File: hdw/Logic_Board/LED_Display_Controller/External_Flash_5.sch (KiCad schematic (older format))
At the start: 16 parts, among them U2201 SST25PF020B

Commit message: Added some digikey partnumbers to components
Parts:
- C2201: footprint (none) -> Capacitors_SMD:C_0603; Digi-Key PN PN -> 311-1344-1-ND; Voltage 25V -> 50V
- C2202: Digi-Key PN PN -> 1276-1921-1-ND; Voltage 25V -> 50V
- C2203: Digi-Key PN PN -> 1276-1018-1-ND; Voltage 25V -> 50V
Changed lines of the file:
@@
 F 0 "C2201" H 5815 5530 50  0000 L CNN
 F 1 "0.1uF" H 5815 5330 50  0000 L CNN
-F 2 "" H 5828 5280 50  0001 C CNN
+F 2 "Capacitors_SMD:C_0603" H 5828 5280 50  0001 C CNN
 F 3 "" H 5815 5530 50  0001 C CNN
 F 4 "0603" H 5640 5530 50  0000 R CNN "display_footprint"
-F 5 "25V" H 5640 5430 50  0000 R CNN "Voltage"
+F 5 "50V" H 5640 5430 50  0000 R CNN "Voltage"
 F 6 "X7R" H 5640 5330 50  0000 R CNN "Dielectric"
-F 7 "PN" H 6215 5930 60  0001 C CNN "Digi-Key PN"
+F 7 "311-1344-1-ND" H 6215 5930 60  0001 C CNN "Digi-Key PN"
 	1    5790 5430
 	1    0    0    -1
@@
 F 3 "" H 6115 5530 50  0001 C CNN
 F 4 "0603" H 5940 5530 50  0001 R CNN "display_footprint"
-F 5 "25V" H 5940 5430 50  0001 R CNN "Voltage"
+F 5 "50V" H 5940 5430 50  0001 R CNN "Voltage"
 F 6 "X7R" H 5940 5330 50  0001 R CNN "Dielectric"
-F 7 "PN" H 6515 5930 60  0001 C CNN "Digi-Key PN"
+F 7 "1276-1921-1-ND" H 6515 5930 60  0001 C CNN "Digi-Key PN"
 	1    6090 5430
 	1    0    0    -1
@@
 F 3 "" H 6415 5530 50  0001 C CNN
 F 4 "0603" H 6240 5530 50  0001 R CNN "display_footprint"
-F 5 "25V" H 6240 5430 50  0001 R CNN "Voltage"
+F 5 "50V" H 6240 5430 50  0001 R CNN "Voltage"
 F 6 "X7R" H 6240 5330 50  0001 R CNN "Dielectric"
-F 7 "PN" H 6815 5930 60  0001 C CNN "Digi-Key PN"
+F 7 "1276-1018-1-ND" H 6815 5930 60  0001 C CNN "Digi-Key PN"
 	1    6390 5430
 	1    0    0    -1

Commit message: Finished first pass of digikey part numbers
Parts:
- R2201, R2202, R2203, R2204, R2205, R2212: Digi-Key PN PN -> A106047CT-ND
- R2206, R2207, R2208, R2209, R2210, R2211: Digi-Key PN PN -> RMCF0603FT10K0CT-ND
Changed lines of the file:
@@
 F 5 "1%" H 5410 4320 50  0000 L CNN "Tolerance"
 F 6 "1/10W" H 5410 4240 50  0000 L CNN "Wattage"
-F 7 "PN" H 5630 4720 60  0001 C CNN "Digi-Key PN"
+F 7 "RMCF0603FT10K0CT-ND" H 5630 4720 60  0001 C CNN "Digi-Key PN"
 	1    5330 4320
 	1    0    0    -1
@@
 F 5 "1%" H 4600 4320 50  0000 L CNN "Tolerance"
 F 6 "1/10W" H 4600 4240 50  0000 L CNN "Wattage"
-F 7 "PN" H 4820 4720 60  0001 C CNN "Digi-Key PN"
+F 7 "RMCF0603FT10K0CT-ND" H 4820 4720 60  0001 C CNN "Digi-Key PN"
 	1    4520 4320
 	1    0    0    -1
@@
 F 5 "1%" H 5190 3130 50  0000 L CNN "Tolerance"
 F 6 "1/10W" H 5190 3050 50  0000 L CNN "Wattage"
-F 7 "PN" H 5410 3530 60  0001 C CNN "Digi-Key PN"
+F 7 "RMCF0603FT10K0CT-ND" H 5410 3530 60  0001 C CNN "Digi-Key PN"
 	1    5110 3130
 	1    0    0    -1
@@
 F 5 "1%" H 4600 3130 50  0000 L CNN "Tolerance"
 F 6 "1/10W" H 4600 3050 50  0000 L CNN "Wattage"
-F 7 "PN" H 4820 3530 60  0001 C CNN "Digi-Key PN"
+F 7 "RMCF0603FT10K0CT-ND" H 4820 3530 60  0001 C CNN "Digi-Key PN"
 	1    4520 3130
 	1    0    0    -1
@@
 F 5 "1%" H 4010 3130 50  0000 L CNN "Tolerance"
 F 6 "1/10W" H 4010 3050 50  0000 L CNN "Wattage"
-F 7 "PN" H 4230 3530 60  0001 C CNN "Digi-Key PN"
+F 7 "RMCF0603FT10K0CT-ND" H 4230 3530 60  0001 C CNN "Digi-Key PN"
 	1    3930 3130
 	1    0    0    -1
@@
 F 5 "1%" H 6830 3850 50  0000 L CNN "Tolerance"
 F 6 "1/10W" H 6830 3770 50  0000 L CNN "Wattage"
-F 7 "PN" H 7050 4250 60  0001 C CNN "Digi-Key PN"
+F 7 "RMCF0603FT10K0CT-ND" H 7050 4250 60  0001 C CNN "Digi-Key PN"
 	1    6750 3850
 	1    0    0    -1
@@
 F 5 "1%" V 3620 3450 50  0001 C CNN "Tolerance"
 F 6 "1/10W" V 3720 3450 50  0001 C CNN "Wattage"
-F 7 "PN" H 3720 3850 60  0001 C CNN "Digi-Key PN"
+F 7 "A106047CT-ND" H 3720 3850 60  0001 C CNN "Digi-Key PN"
 	1    3420 3450
 	0    1    1    0
@@
 F 5 "1%" V 7330 3450 50  0001 C CNN "Tolerance"
 F 6 "1/10W" V 7430 3450 50  0001 C CNN "Wattage"
-F 7 "PN" H 7430 3850 60  0001 C CNN "Digi-Key PN"
+F 7 "A106047CT-ND" H 7430 3850 60  0001 C CNN "Digi-Key PN"
 	1    7130 3450
 	0    1    1    0
@@
 F 5 "1%" V 3620 3550 50  0001 C CNN "Tolerance"
 F 6 "1/10W" V 3720 3550 50  0001 C CNN "Wattage"
-F 7 "PN" H 3720 3950 60  0001 C CNN "Digi-Key PN"
+F 7 "A106047CT-ND" H 3720 3950 60  0001 C CNN "Digi-Key PN"
 	1    3420 3550
 	0    1    1    0
@@
 F 5 "1%" V 3620 3750 50  0001 C CNN "Tolerance"
 F 6 "1/10W" V 3720 3750 50  0001 C CNN "Wattage"
-F 7 "PN" H 3720 4150 60  0001 C CNN "Digi-Key PN"
+F 7 "A106047CT-ND" H 3720 4150 60  0001 C CNN "Digi-Key PN"
 	1    3420 3750
 	0    1    1    0
@@
 F 5 "1%" V 3620 3850 50  0001 C CNN "Tolerance"
 F 6 "1/10W" V 3720 3850 50  0001 C CNN "Wattage"
-F 7 "PN" H 3720 4250 60  0001 C CNN "Digi-Key PN"
+F 7 "A106047CT-ND" H 3720 4250 60  0001 C CNN "Digi-Key PN"
 	1    3420 3850
 	0    1    1    0
@@
 F 5 "1%" V 3620 3650 50  0001 C CNN "Tolerance"
 F 6 "1/10W" V 3720 3650 50  0001 C CNN "Wattage"
-F 7 "PN" H 3720 4050 60  0001 C CNN "Digi-Key PN"
+F 7 "A106047CT-ND" H 3720 4050 60  0001 C CNN "Digi-Key PN"
 	1    3420 3650
 	0    1    1    0

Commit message: First pass assignment of footprints to all components
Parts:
- C2202, C2203: footprint (none) -> Capacitors_SMD:C_0603
- R2201, R2202, R2203, R2204, R2205, R2206, R2207, R2208, R2209, R2210, R2211, R2212: footprint (none) -> Resistors_SMD:R_0603
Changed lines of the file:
@@
 F 0 "R2210" H 5270 4320 50  0000 R CNN
 F 1 "10k" V 5330 4320 50  0000 C CNN
-F 2 "" H 5330 4320 50  0001 C CNN
+F 2 "Resistors_SMD:R_0603" H 5330 4320 50  0001 C CNN
 F 3 "" H 5330 4320 50  0001 C CNN
 F 4 "0603" H 5410 4400 50  0000 L CNN "display_footprint"
@@
 F 0 "R2208" H 4460 4320 50  0000 R CNN
 F 1 "10k" V 4520 4320 50  0000 C CNN
-F 2 "" H 4520 4320 50  0001 C CNN
+F 2 "Resistors_SMD:R_0603" H 4520 4320 50  0001 C CNN
 F 3 "" H 4520 4320 50  0001 C CNN
 F 4 "0603" H 4600 4400 50  0000 L CNN "display_footprint"
@@
 F 0 "R2209" H 5050 3130 50  0000 R CNN
 F 1 "10k" V 5110 3130 50  0000 C CNN
-F 2 "" H 5110 3130 50  0001 C CNN
+F 2 "Resistors_SMD:R_0603" H 5110 3130 50  0001 C CNN
 F 3 "" H 5110 3130 50  0001 C CNN
 F 4 "0603" H 5190 3210 50  0000 L CNN "display_footprint"
@@
 F 0 "R2207" H 4460 3130 50  0000 R CNN
 F 1 "10k" V 4520 3130 50  0000 C CNN
-F 2 "" H 4520 3130 50  0001 C CNN
+F 2 "Resistors_SMD:R_0603" H 4520 3130 50  0001 C CNN
 F 3 "" H 4520 3130 50  0001 C CNN
 F 4 "0603" H 4600 3210 50  0000 L CNN "display_footprint"
@@
 F 0 "R2206" H 3870 3130 50  0000 R CNN
 F 1 "10k" V 3930 3130 50  0000 C CNN
-F 2 "" H 3930 3130 50  0001 C CNN
+F 2 "Resistors_SMD:R_0603" H 3930 3130 50  0001 C CNN
 F 3 "" H 3930 3130 50  0001 C CNN
 F 4 "0603" H 4010 3210 50  0000 L CNN "display_footprint"
@@
 F 0 "R2211" H 6690 3850 50  0000 R CNN
 F 1 "10k" V 6750 3850 50  0000 C CNN
-F 2 "" H 6750 3850 50  0001 C CNN
+F 2 "Resistors_SMD:R_0603" H 6750 3850 50  0001 C CNN
 F 3 "" H 6750 3850 50  0001 C CNN
 F 4 "0603" H 6830 3930 50  0000 L CNN "display_footprint"
@@
 F 0 "R2201" V 3380 3580 50  0000 L CNN
 F 1 "100" V 3420 3450 50  0000 C CNN
-F 2 "" H 3420 3450 50  0001 C CNN
+F 2 "Resistors_SMD:R_0603" H 3420 3450 50  0001 C CNN
 F 3 "" H 3420 3450 50  0001 C CNN
 F 4 "0603" V 3520 3450 50  0001 C CNN "display_footprint"
@@
 F 0 "R2212" V 7030 3450 50  0000 C CNN
 F 1 "100" V 7130 3450 50  0000 C CNN
-F 2 "" H 7130 3450 50  0001 C CNN
+F 2 "Resistors_SMD:R_0603" H 7130 3450 50  0001 C CNN
 F 3 "" H 7130 3450 50  0001 C CNN
 F 4 "0603" V 7230 3450 50  0001 C CNN "display_footprint"
@@
 F 0 "C2202" H 6115 5530 50  0000 L CNN
 F 1 "10nF" H 6115 5330 50  0000 L CNN
-F 2 "" H 6128 5280 50  0001 C CNN
+F 2 "Capacitors_SMD:C_0603" H 6128 5280 50  0001 C CNN
 F 3 "" H 6115 5530 50  0001 C CNN
 F 4 "0603" H 5940 5530 50  0001 R CNN "display_footprint"
@@
 F 0 "C2203" H 6415 5530 50  0000 L CNN
 F 1 "1nF" H 6415 5330 50  0000 L CNN
-F 2 "" H 6428 5280 50  0001 C CNN
+F 2 "Capacitors_SMD:C_0603" H 6428 5280 50  0001 C CNN
 F 3 "" H 6415 5530 50  0001 C CNN
 F 4 "0603" H 6240 5530 50  0001 R CNN "display_footprint"
@@
 F 0 "R2202" V 3380 3680 50  0000 L CNN
 F 1 "100" V 3420 3550 50  0000 C CNN
-F 2 "" H 3420 3550 50  0001 C CNN
+F 2 "Resistors_SMD:R_0603" H 3420 3550 50  0001 C CNN
 F 3 "" H 3420 3550 50  0001 C CNN
 F 4 "0603" V 3520 3550 50  0001 C CNN "display_footprint"
@@
 F 0 "R2204" V 3380 3880 50  0000 L CNN
 F 1 "100" V 3420 3750 50  0000 C CNN
-F 2 "" H 3420 3750 50  0001 C CNN
+F 2 "Resistors_SMD:R_0603" H 3420 3750 50  0001 C CNN
 F 3 "" H 3420 3750 50  0001 C CNN
 F 4 "0603" V 3520 3750 50  0001 C CNN "display_footprint"
@@
 F 0 "R2205" V 3380 3980 50  0000 L CNN
 F 1 "100" V 3420 3850 50  0000 C CNN
-F 2 "" H 3420 3850 50  0001 C CNN
+F 2 "Resistors_SMD:R_0603" H 3420 3850 50  0001 C CNN
 F 3 "" H 3420 3850 50  0001 C CNN
 F 4 "0603" V 3520 3850 50  0001 C CNN "display_footprint"
@@
 F 0 "R2203" V 3380 3780 50  0000 L CNN
 F 1 "100" V 3420 3650 50  0000 C CNN
-F 2 "" H 3420 3650 50  0001 C CNN
+F 2 "Resistors_SMD:R_0603" H 3420 3650 50  0001 C CNN
 F 3 "" H 3420 3650 50  0001 C CNN
 F 4 "0603" V 3520 3650 50  0001 C CNN "display_footprint"

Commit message: Resolved a few library dependencies
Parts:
- R2201, R2202, R2203, R2204, R2205, R2206, R2207, R2208, R2209, R2210, R2211, R2212: symbol Custom_Library:R_Custom -> LED_Display_Local_Library:R_Custom
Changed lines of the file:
@@
 $EndComp
 $Comp
-L Custom_Library:R_Custom R2210
+L LED_Display_Local_Library:R_Custom R2210
 U 1 1 5BBE9655
 P 5330 4320
@@
 $EndComp
 $Comp
-L Custom_Library:R_Custom R2208
+L LED_Display_Local_Library:R_Custom R2208
 U 1 1 5BBE9660
 P 4520 4320
@@
 $EndComp
 $Comp
-L Custom_Library:R_Custom R2209
+L LED_Display_Local_Library:R_Custom R2209
 U 1 1 5BBE966B
 P 5110 3130
@@
 $EndComp
 $Comp
-L Custom_Library:R_Custom R2207
+L LED_Display_Local_Library:R_Custom R2207
 U 1 1 5BBE9676
 P 4520 3130
@@
 $EndComp
 $Comp
-L Custom_Library:R_Custom R2206
+L LED_Display_Local_Library:R_Custom R2206
 U 1 1 5BBE9681
 P 3930 3130
@@
 $EndComp
 $Comp
-L Custom_Library:R_Custom R2211
+L LED_Display_Local_Library:R_Custom R2211
 U 1 1 5BBE968C
 P 6750 3850
@@
 $EndComp
 $Comp
-L Custom_Library:R_Custom R2201
+L LED_Display_Local_Library:R_Custom R2201
 U 1 1 5BBE96BB
 P 3420 3450
@@
 FLASH_SCK
 $Comp
-L Custom_Library:R_Custom R2212
+L LED_Display_Local_Library:R_Custom R2212
 U 1 1 5BBE96E8
 P 7130 3450
@@
 	6090 5240 6390 5240
 $Comp
-L Custom_Library:R_Custom R2202
+L LED_Display_Local_Library:R_Custom R2202
 U 1 1 5BBE9733
 P 3420 3550
@@
 $EndComp
 $Comp
-L Custom_Library:R_Custom R2204
+L LED_Display_Local_Library:R_Custom R2204
 U 1 1 5BBE973E
 P 3420 3750
@@
 $EndComp
 $Comp
-L Custom_Library:R_Custom R2205
+L LED_Display_Local_Library:R_Custom R2205
 U 1 1 5BBE9749
 P 3420 3850
@@
 ~FLASH_Hold
 $Comp
-L Custom_Library:R_Custom R2203
+L LED_Display_Local_Library:R_Custom R2203
 U 1 1 5BC1DF14
 P 3420 3650

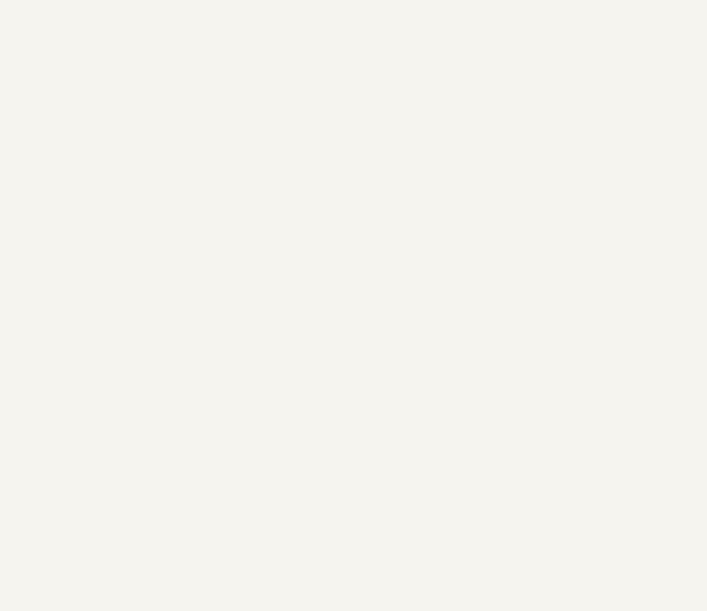
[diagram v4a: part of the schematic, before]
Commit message: Added flash chip select LEDs
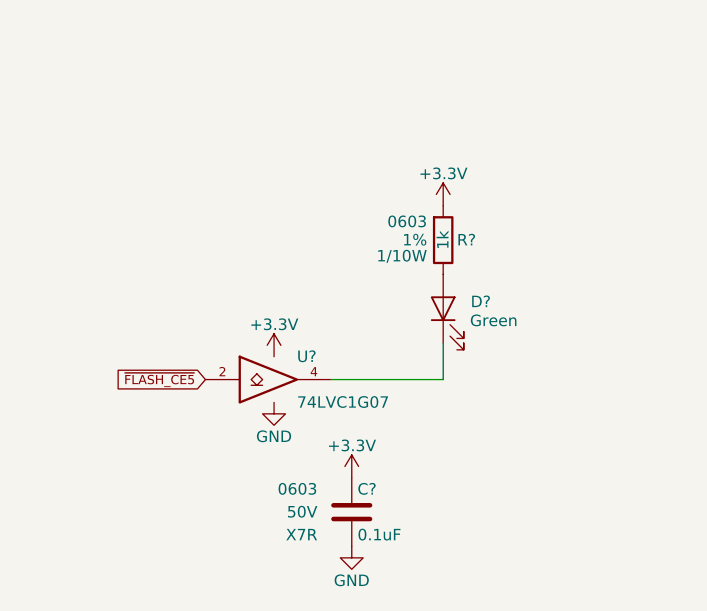
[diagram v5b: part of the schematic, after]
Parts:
- added C?: 0.1uF, Capacitors_SMD:C_0603, symbol LED_Display_Local_Library:C_Custom
- added D?: Green, LEDs:LED_0603, symbol Device:LED
- added R?: 1k, Resistors_SMD:R_0603, symbol LED_Display_Local_Library:R_Custom
- added U?: 74LVC1G07, TO_SOT_Packages_SMD:SOT-353_SC-70-5, symbol LED_Display_Local_Library:74LVC1G07_Power
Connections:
- net +3V3: now also C?.1, R?.1, U?.5 (VCC)
- net GND: now also C?.2, U?.3 (GND)
- net ~FLASH_CE5: now also U?.2
- new net: D?.1 (K), U?.4
- new net: D?.2 (A), R?.2
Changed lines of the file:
@@
 Wire Wire Line
 	4520 3850 5680 3850
+$Comp
+L LED_Display_Local_Library:C_Custom C?
+U 1 1 5C172D4E
+P 2010 6900
+AR Path="/5BAAE16C/5C172D4E" Ref="C?"  Part="1"
+AR Path="/5BB181D8/5C172D4E" Ref="C?"  Part="1"
+AR Path="/5BB2595E/5C172D4E" Ref="C?"  Part="1"
+AR Path="/5BB25AF0/5C172D4E" Ref="C?"  Part="1"
+F 0 "C?" H 2035 7000 50  0000 L CNN
+F 1 "0.1uF" H 2035 6800 50  0000 L CNN
+F 2 "Capacitors_SMD:C_0603" H 2048 6750 50  0001 C CNN
+F 3 "" H 2035 7000 50  0001 C CNN
+F 4 "0603" H 1860 7000 50  0000 R CNN "display_footprint"
+F 5 "50V" H 1860 6900 50  0000 R CNN "Voltage"
+F 6 "X7R" H 1860 6800 50  0000 R CNN "Dielectric"
+F 7 "311-1344-1-ND" H 2435 7400 60  0001 C CNN "Digi-Key PN"
+	1    2010 6900
+	1    0    0    -1
+$EndComp
+$Comp
+L LED_Display_Local_Library:74LVC1G07_Power U?
+U 1 1 5C172D56
+P 1670 6320
+AR Path="/5BB2595E/5C172D56" Ref="U?"  Part="1"
+AR Path="/5BB25AF0/5C172D56" Ref="U?"  Part="1"
+F 0 "U?" H 1770 6420 50  0000 L CNN
+F 1 "74LVC1G07" H 1770 6220 50  0000 L CNN
+F 2 "TO_SOT_Packages_SMD:SOT-353_SC-70-5" H 1670 6320 50  0001 C CNN
+F 3 "http://www.ti.com/lit/sg/scyt129e/scyt129e.pdf" H 1670 6320 50  0001 C CNN
+F 4 "296-8486-1-ND" H 1670 6320 50  0001 C CNN "Digi-Key PN"
+	1    1670 6320
+	1    0    0    -1
+$EndComp
+$Comp
+L power:+3.3V #PWR?
+U 1 1 5C172D5D
+P 1670 6220
+AR Path="/5BB2595E/5C172D5D" Ref="#PWR?"  Part="1"
+AR Path="/5BB25AF0/5C172D5D" Ref="#PWR?"  Part="1"
+F 0 "#PWR?" H 1670 6070 50  0001 C CNN
+F 1 "+3.3V" H 1670 6360 50  0000 C CNN
+F 2 "" H 1670 6220 50  0001 C CNN
+F 3 "" H 1670 6220 50  0001 C CNN
+	1    1670 6220
+	1    0    0    -1
+$EndComp
+$Comp
+L power:+3.3V #PWR?
+U 1 1 5C172D63
+P 2010 6750
+AR Path="/5BB2595E/5C172D63" Ref="#PWR?"  Part="1"
+AR Path="/5BB25AF0/5C172D63" Ref="#PWR?"  Part="1"
+F 0 "#PWR?" H 2010 6600 50  0001 C CNN
+F 1 "+3.3V" H 2010 6890 50  0000 C CNN
+F 2 "" H 2010 6750 50  0001 C CNN
+F 3 "" H 2010 6750 50  0001 C CNN
+	1    2010 6750
+	1    0    0    -1
+$EndComp
+$Comp
+L power:GND #PWR?
+U 1 1 5C172D69
+P 2010 7050
+AR Path="/5BB2595E/5C172D69" Ref="#PWR?"  Part="1"
+AR Path="/5BB25AF0/5C172D69" Ref="#PWR?"  Part="1"
+F 0 "#PWR?" H 2010 6800 50  0001 C CNN
+F 1 "GND" H 2010 6900 50  0000 C CNN
+F 2 "" H 2010 7050 50  0001 C CNN
+F 3 "" H 2010 7050 50  0001 C CNN
+	1    2010 7050
+	1    0    0    -1
+$EndComp
+$Comp
+L power:GND #PWR?
+U 1 1 5C172D6F
+P 1670 6420
+AR Path="/5BB2595E/5C172D6F" Ref="#PWR?"  Part="1"
+AR Path="/5BB25AF0/5C172D6F" Ref="#PWR?"  Part="1"
+F 0 "#PWR?" H 1670 6170 50  0001 C CNN
+F 1 "GND" H 1670 6270 50  0000 C CNN
+F 2 "" H 1670 6420 50  0001 C CNN
+F 3 "" H 1670 6420 50  0001 C CNN
+	1    1670 6420
+	1    0    0    -1
+$EndComp
+Text GLabel 1370 6320 0    40   Input ~ 0
+~FLASH_CE5
+$Comp
+L power:+3.3V #PWR?
+U 1 1 5C172D76
+P 2410 5560
+AR Path="/5BB844FD/5C172D76" Ref="#PWR?"  Part="1"
+AR Path="/5BF346B3/5C172D76" Ref="#PWR?"  Part="1"
+AR Path="/5BB2595E/5C172D76" Ref="#PWR?"  Part="1"
+AR Path="/5BB25AF0/5C172D76" Ref="#PWR?"  Part="1"
+F 0 "#PWR?" H 2410 5410 50  0001 C CNN
+F 1 "+3.3V" H 2410 5700 50  0000 C CNN
+F 2 "" H 2410 5560 50  0001 C CNN
+F 3 "" H 2410 5560 50  0001 C CNN
+	1    2410 5560
+	1    0    0    -1
+$EndComp
+Wire Wire Line
+	1920 6320 2410 6320
+Wire Wire Line
+	2410 6320 2410 6160
+$Comp
+L LED_Display_Local_Library:R_Custom R?
+U 1 1 5C172D82
+P 2410 5710
+AR Path="/5BAAE1F3/5C172D82" Ref="R?"  Part="1"
+AR Path="/5BAAE1DC/5C172D82" Ref="R?"  Part="1"
+AR Path="/5BAAE16C/5C172D82" Ref="R?"  Part="1"
+AR Path="/5BB844FD/5C172D82" Ref="R?"  Part="1"
+AR Path="/5BF346B3/5C172D82" Ref="R?"  Part="1"
+AR Path="/5BB2595E/5C172D82" Ref="R?"  Part="1"
+AR Path="/5BB25AF0/5C172D82" Ref="R?"  Part="1"
+F 0 "R?" H 2350 5710 50  0000 R CNN
+F 1 "1k" V 2410 5710 50  0000 C CNN
+F 2 "Resistors_SMD:R_0603" H 2410 5710 50  0001 C CNN
+F 3 "" H 2410 5710 50  0001 C CNN
+F 4 "0603" H 2480 5790 50  0000 L CNN "display_footprint"
+F 5 "1%" H 2480 5710 50  0000 L CNN "Tolerance"
+F 6 "1/10W" H 2480 5640 50  0000 L CNN "Wattage"
+F 7 "RMCF0603FT1K00CT-ND" H 2710 6110 60  0001 C CNN "Digi-Key PN"
+	1    2410 5710
+	-1   0    0    -1
+$EndComp
+$Comp
+L Device:LED D?
+U 1 1 5C172D8A
+P 2410 6010
+AR Path="/5BB844FD/5C172D8A" Ref="D?"  Part="1"
+AR Path="/5BF346B3/5C172D8A" Ref="D?"  Part="1"
+AR Path="/5BB2595E/5C172D8A" Ref="D?"  Part="1"
+AR Path="/5BB25AF0/5C172D8A" Ref="D?"  Part="1"
+F 0 "D?" V 2440 5890 50  0000 R CNN
+F 1 "Green" V 2357 5893 50  0000 R CNN
+F 2 "LEDs:LED_0603" H 2410 6010 50  0001 C CNN
+F 3 "~" H 2410 6010 50  0001 C CNN
+F 4 "160-1446-1-ND" H -2600 3010 50  0001 C CNN "Digi-Key PN"
+	1    2410 6010
+	0    -1   -1   0
+$EndComp
 $EndSCHEMATC

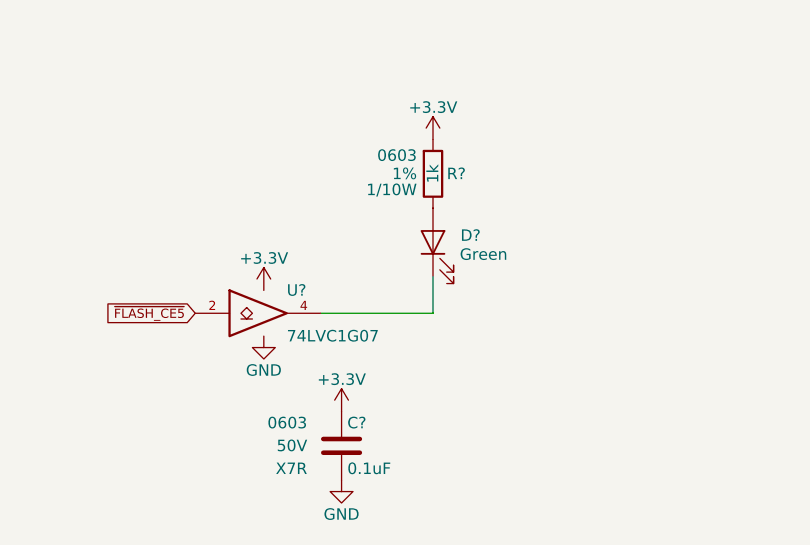
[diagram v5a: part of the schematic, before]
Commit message: Added WIFI comm LED
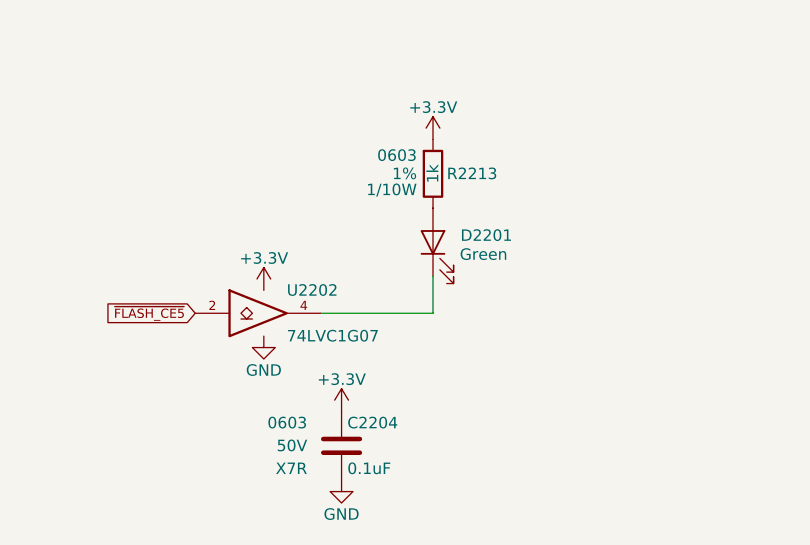
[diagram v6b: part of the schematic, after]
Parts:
- gave numbers to parts that had none: 4
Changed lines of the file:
@@
 AR Path="/5BB181D8/5C172D4E" Ref="C?"  Part="1"
 AR Path="/5BB2595E/5C172D4E" Ref="C?"  Part="1"
-AR Path="/5BB25AF0/5C172D4E" Ref="C?"  Part="1"
-F 0 "C?" H 2035 7000 50  0000 L CNN
+AR Path="/5BB25AF0/5C172D4E" Ref="C2204"  Part="1"
+F 0 "C2204" H 2035 7000 50  0000 L CNN
 F 1 "0.1uF" H 2035 6800 50  0000 L CNN
 F 2 "Capacitors_SMD:C_0603" H 2048 6750 50  0001 C CNN
@@
 P 1670 6320
 AR Path="/5BB2595E/5C172D56" Ref="U?"  Part="1"
-AR Path="/5BB25AF0/5C172D56" Ref="U?"  Part="1"
-F 0 "U?" H 1770 6420 50  0000 L CNN
+AR Path="/5BB25AF0/5C172D56" Ref="U2202"  Part="1"
+F 0 "U2202" H 1770 6420 50  0000 L CNN
 F 1 "74LVC1G07" H 1770 6220 50  0000 L CNN
 F 2 "TO_SOT_Packages_SMD:SOT-353_SC-70-5" H 1670 6320 50  0001 C CNN
@@
 P 1670 6220
 AR Path="/5BB2595E/5C172D5D" Ref="#PWR?"  Part="1"
-AR Path="/5BB25AF0/5C172D5D" Ref="#PWR?"  Part="1"
-F 0 "#PWR?" H 1670 6070 50  0001 C CNN
+AR Path="/5BB25AF0/5C172D5D" Ref="#PWR02211"  Part="1"
+F 0 "#PWR02211" H 1670 6070 50  0001 C CNN
 F 1 "+3.3V" H 1670 6360 50  0000 C CNN
 F 2 "" H 1670 6220 50  0001 C CNN
@@
 P 2010 6750
 AR Path="/5BB2595E/5C172D63" Ref="#PWR?"  Part="1"
-AR Path="/5BB25AF0/5C172D63" Ref="#PWR?"  Part="1"
-F 0 "#PWR?" H 2010 6600 50  0001 C CNN
+AR Path="/5BB25AF0/5C172D63" Ref="#PWR02213"  Part="1"
+F 0 "#PWR02213" H 2010 6600 50  0001 C CNN
 F 1 "+3.3V" H 2010 6890 50  0000 C CNN
 F 2 "" H 2010 6750 50  0001 C CNN
@@
 P 2010 7050
 AR Path="/5BB2595E/5C172D69" Ref="#PWR?"  Part="1"
-AR Path="/5BB25AF0/5C172D69" Ref="#PWR?"  Part="1"
-F 0 "#PWR?" H 2010 6800 50  0001 C CNN
+AR Path="/5BB25AF0/5C172D69" Ref="#PWR02214"  Part="1"
+F 0 "#PWR02214" H 2010 6800 50  0001 C CNN
 F 1 "GND" H 2010 6900 50  0000 C CNN
 F 2 "" H 2010 7050 50  0001 C CNN
@@
 P 1670 6420
 AR Path="/5BB2595E/5C172D6F" Ref="#PWR?"  Part="1"
-AR Path="/5BB25AF0/5C172D6F" Ref="#PWR?"  Part="1"
-F 0 "#PWR?" H 1670 6170 50  0001 C CNN
+AR Path="/5BB25AF0/5C172D6F" Ref="#PWR02212"  Part="1"
+F 0 "#PWR02212" H 1670 6170 50  0001 C CNN
 F 1 "GND" H 1670 6270 50  0000 C CNN
 F 2 "" H 1670 6420 50  0001 C CNN
@@
 AR Path="/5BF346B3/5C172D76" Ref="#PWR?"  Part="1"
 AR Path="/5BB2595E/5C172D76" Ref="#PWR?"  Part="1"
-AR Path="/5BB25AF0/5C172D76" Ref="#PWR?"  Part="1"
-F 0 "#PWR?" H 2410 5410 50  0001 C CNN
+AR Path="/5BB25AF0/5C172D76" Ref="#PWR02215"  Part="1"
+F 0 "#PWR02215" H 2410 5410 50  0001 C CNN
 F 1 "+3.3V" H 2410 5700 50  0000 C CNN
 F 2 "" H 2410 5560 50  0001 C CNN
@@
 AR Path="/5BF346B3/5C172D82" Ref="R?"  Part="1"
 AR Path="/5BB2595E/5C172D82" Ref="R?"  Part="1"
-AR Path="/5BB25AF0/5C172D82" Ref="R?"  Part="1"
-F 0 "R?" H 2350 5710 50  0000 R CNN
+AR Path="/5BB25AF0/5C172D82" Ref="R2213"  Part="1"
+F 0 "R2213" H 2350 5710 50  0000 R CNN
 F 1 "1k" V 2410 5710 50  0000 C CNN
 F 2 "Resistors_SMD:R_0603" H 2410 5710 50  0001 C CNN
@@
 AR Path="/5BF346B3/5C172D8A" Ref="D?"  Part="1"
 AR Path="/5BB2595E/5C172D8A" Ref="D?"  Part="1"
-AR Path="/5BB25AF0/5C172D8A" Ref="D?"  Part="1"
-F 0 "D?" V 2440 5890 50  0000 R CNN
+AR Path="/5BB25AF0/5C172D8A" Ref="D2201"  Part="1"
+F 0 "D2201" V 2440 5890 50  0000 R CNN
 F 1 "Green" V 2357 5893 50  0000 R CNN
 F 2 "LEDs:LED_0603" H 2410 6010 50  0001 C CNN
